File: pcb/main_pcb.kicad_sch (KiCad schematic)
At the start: 34 parts, among them J1 Conn_01x06_Socket, J2 Conn_01x10_Pin, J3 Conn_01x06_Pin, J4 USB_C_Receptacle_USB2.0, Q1 Si2323DS, SW1 SW_Push, SW2 SW_Push, SW3 SW_Push, U1 ESP32-H2-MINI-1, U2 LM5165Y

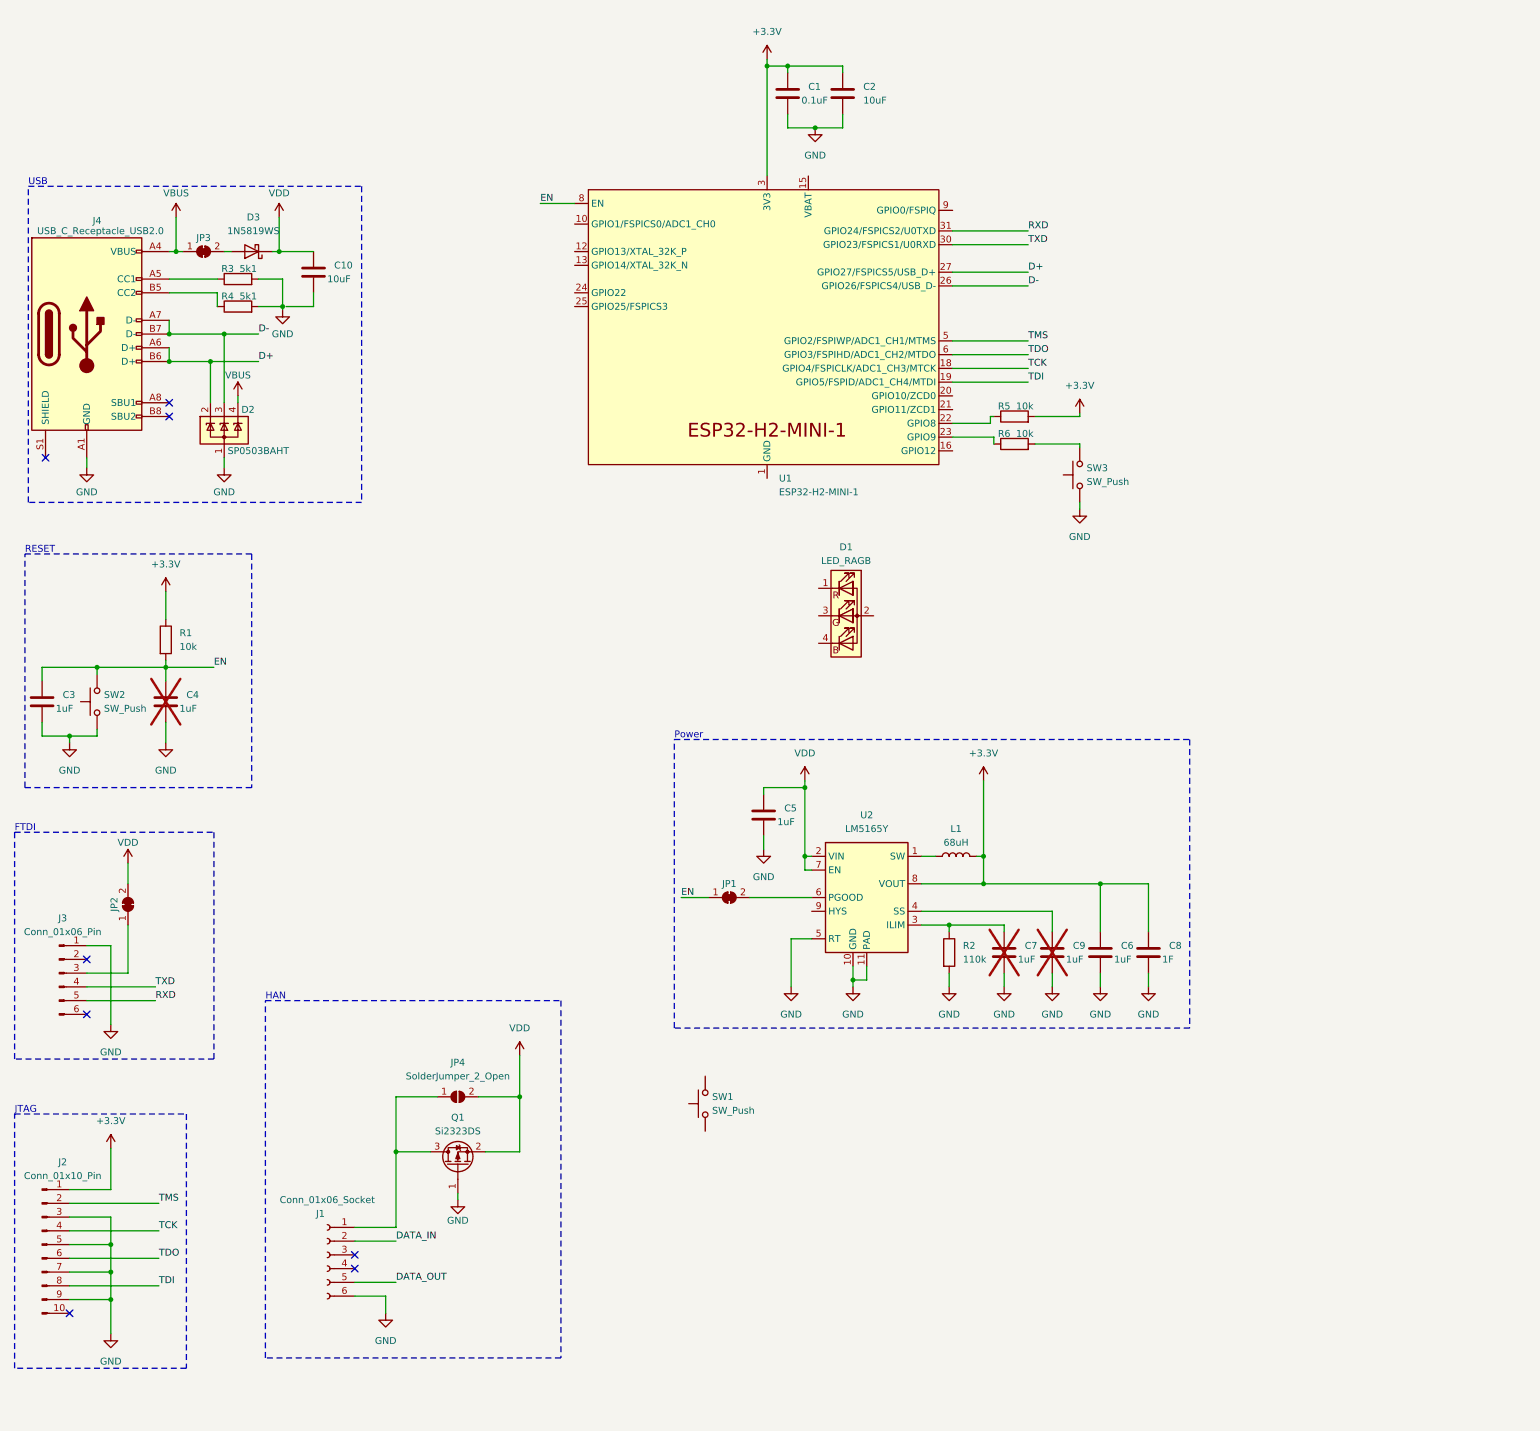
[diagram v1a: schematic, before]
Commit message: Add pair button circuit
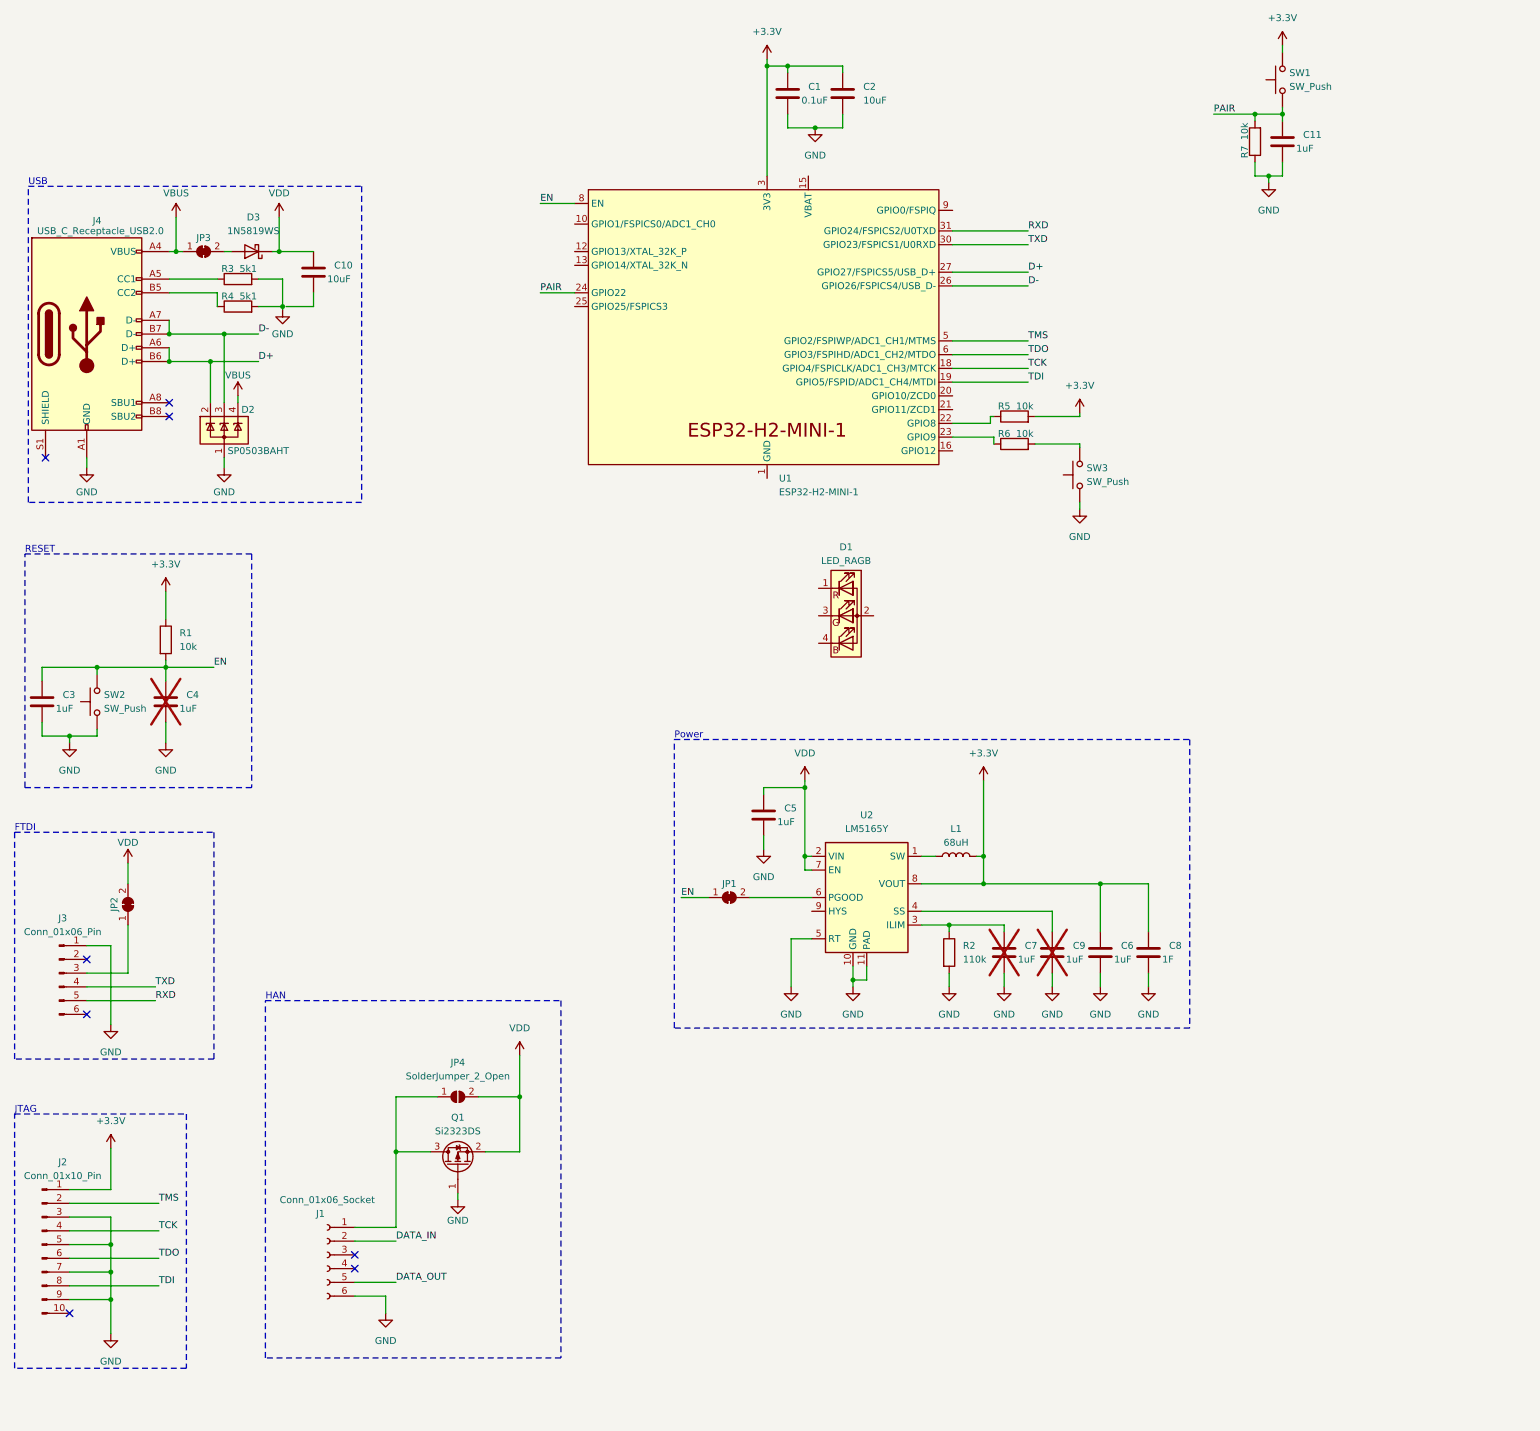
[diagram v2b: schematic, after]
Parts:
- added C11: 1uF, Capacitor_SMD:C_1206_3216Metric_Pad1.33x1.80mm_HandSolder, symbol Device:C
- added R7: 10k, Resistor_SMD:R_1206_3216Metric_Pad1.30x1.75mm_HandSolder, symbol Device:R
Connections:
- net +3.3V: now also SW1.2
- net GND: now also C11.2, R7.1
- net PAIR: now reaches U1.24 (GPIO22)
- net PAIR: now also SW1.1, C11.1, R7.2
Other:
- moved on the sheet: SW1
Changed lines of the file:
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@@
   (junction (at 34.925 140.335) (diameter 0) (color 0 0 0 0)
   )
+  (junction (at 251.46 49.53) (diameter 0) (color 0 0 0 0)
+  )
+  (junction (at 248.92 38.1) (diameter 0) (color 0 0 0 0)
+  )
   (junction (at 198.755 175.26) (diameter 0) (color 0 0 0 0)
   )
@@
   )
   (junction (at 58.42 78.74) (diameter 0) (color 0 0 0 0)
+  )
+  (junction (at 254 38.1) (diameter 0) (color 0 0 0 0)
   )
   (junction (at 198.755 180.34) (diameter 0) (color 0 0 0 0)
@@
     (stroke (width 0) (type default))
   )
+  (wire (pts (xy 254 46.99) (xy 254 49.53))
+    (stroke (width 0) (type default))
+  )
   (wire (pts (xy 58.42 78.74) (xy 58.42 91.44))
     (stroke (width 0) (type default))
@@
     (stroke (width 0) (type default))
   )
+  (wire (pts (xy 248.92 49.53) (xy 251.46 49.53))
+    (stroke (width 0) (type default))
+  )
   (wire (pts (xy 200.025 93.98) (xy 200.025 95.25))
     (stroke (width 0) (type default))
@@
     (stroke (width 0) (type default))
   )
+  (wire (pts (xy 116.84 71.12) (xy 123.19 71.12))
+    (stroke (width 0) (type default))
+  )
   (wire (pts (xy 67.31 63.5) (xy 68.58 63.5))
     (stroke (width 0) (type default))
@@
     (stroke (width 0) (type default))
   )
+  (wire (pts (xy 248.92 38.1) (xy 254 38.1))
+    (stroke (width 0) (type default))
+  )
   (wire (pts (xy 216.535 99.695) (xy 216.535 99.06))
     (stroke (width 0) (type default))
@@
     (stroke (width 0) (type default))
   )
+  (wire (pts (xy 254 25.4) (xy 254 26.67))
+    (stroke (width 0) (type default))
+  )
   (wire (pts (xy 33.02 191.77) (xy 37.465 191.77))
     (stroke (width 0) (type default))
@@
     (stroke (width 0) (type default))
   )
+  (wire (pts (xy 254 39.37) (xy 254 38.1))
+    (stroke (width 0) (type default))
+  )
   (wire (pts (xy 187.325 180.34) (xy 198.755 180.34))
     (stroke (width 0) (type default))
@@
     (stroke (width 0) (type default))
   )
+  (wire (pts (xy 248.92 39.37) (xy 248.92 38.1))
+    (stroke (width 0) (type default))
+  )
   (wire (pts (xy 48.26 63.5) (xy 49.53 63.5))
     (stroke (width 0) (type default))
@@
     (stroke (width 0) (type default))
   )
+  (wire (pts (xy 248.92 46.99) (xy 248.92 49.53))
+    (stroke (width 0) (type default))
+  )
   (wire (pts (xy 48.26 83.82) (xy 55.88 83.82))
     (stroke (width 0) (type default))
@@
     (stroke (width 0) (type default))
   )
+  (wire (pts (xy 241.3 38.1) (xy 248.92 38.1))
+    (stroke (width 0) (type default))
+  )
   (wire (pts (xy 49.53 63.5) (xy 50.8 63.5))
     (stroke (width 0) (type default))
@@
     (stroke (width 0) (type default))
   )
+  (wire (pts (xy 251.46 49.53) (xy 254 49.53))
+    (stroke (width 0) (type default))
+  )
   (wire (pts (xy 187.325 187.96) (xy 192.405 187.96))
     (stroke (width 0) (type default))
@@
     (stroke (width 0) (type default))
   )
+  (wire (pts (xy 251.46 50.8) (xy 251.46 49.53))
+    (stroke (width 0) (type default))
+  )
   (wire (pts (xy 229.235 189.23) (xy 229.235 180.34))
     (stroke (width 0) (type default))
@@
   )
   (wire (pts (xy 88.265 259.715) (xy 88.265 256.54))
+    (stroke (width 0) (type default))
+  )
+  (wire (pts (xy 254 36.83) (xy 254 38.1))
     (stroke (width 0) (type default))
   )
@@
   )
   (label "EN" (at 56.515 140.335 0) (fields_autoplaced)
+    (effects (font (size 1.27 1.27)) (justify left bottom))
+  )
+  (label "PAIR" (at 241.3 38.1 0) (fields_autoplaced)
+    (effects (font (size 1.27 1.27)) (justify left bottom))
+  )
+  (label "PAIR" (at 116.84 71.12 0) (fields_autoplaced)
     (effects (font (size 1.27 1.27)) (justify left bottom))
   )
@@
     )
   )
+  (symbol (lib_id "power:GND") (at 251.46 50.8 0) (unit 1)
+    (in_bom yes) (on_board yes) (dnp no) (fields_autoplaced)
+    (property "Reference" "#PWR032" (at 251.46 57.15 0)
+      (effects (font (size 1.27 1.27)) hide)
+    )
+    (property "Value" "GND" (at 251.46 55.88 0)
+      (effects (font (size 1.27 1.27)))
+    )
+    (property "Footprint" "" (at 251.46 50.8 0)
+      (effects (font (size 1.27 1.27)) hide)
+    )
+    (property "Datasheet" "" (at 251.46 50.8 0)
+      (effects (font (size 1.27 1.27)) hide)
+    )
+    (pin "1")
+    (instances
+      (project "main_pcb"
+        (path "/6204b7c2-8814-41ee-9243-5078f55f08d4"
+          (reference "#PWR032") (unit 1)
+        )
+      )
+    )
+  )
   (symbol (lib_id "Device:C") (at 211.455 193.04 0) (unit 1)
     (in_bom yes) (on_board yes) (dnp yes)
@@
         (path "/6204b7c2-8814-41ee-9243-5078f55f08d4"
           (reference "C9") (unit 1)
+        )
+      )
+    )
+  )
+  (symbol (lib_id "Device:R") (at 248.92 43.18 180) (unit 1)
+    (in_bom yes) (on_board yes) (dnp no)
+    (property "Reference" "R7" (at 247.015 45.085 90)
+      (effects (font (size 1.27 1.27)))
+    )
+    (property "Value" "10k" (at 247.015 41.275 90)
+      (effects (font (size 1.27 1.27)))
+    )
+    (property "Footprint" "Resistor_SMD:R_1206_3216Metric_Pad1.30x1.75mm_HandSolder" (at 250.698 43.18 90)
+      (effects (font (size 1.27 1.27)) hide)
+    )
+    (property "Datasheet" "~" (at 248.92 43.18 0)
+      (effects (font (size 1.27 1.27)) hide)
+    )
+    (pin "2")
+    (pin "1")
+    (instances
+      (project "main_pcb"
+        (path "/6204b7c2-8814-41ee-9243-5078f55f08d4"
+          (reference "R7") (unit 1)
         )
       )
@@
     )
   )
+  (symbol (lib_id "Device:C") (at 254 43.18 0) (unit 1)
+    (in_bom yes) (on_board yes) (dnp no)
+    (property "Reference" "C11" (at 257.81 41.91 0)
+      (effects (font (size 1.27 1.27)) (justify left))
+    )
+    (property "Value" "1uF" (at 256.54 44.45 0)
+      (effects (font (size 1.27 1.27)) (justify left))
+    )
+    (property "Footprint" "Capacitor_SMD:C_1206_3216Metric_Pad1.33x1.80mm_HandSolder" (at 254.9652 46.99 0)
+      (effects (font (size 1.27 1.27)) hide)
+    )
+    (property "Datasheet" "~" (at 254 43.18 0)
+      (effects (font (size 1.27 1.27)) hide)
+    )
+    (pin "2")
+    (pin "1")
+    (instances
+      (project "main_pcb"
+        (path "/6204b7c2-8814-41ee-9243-5078f55f08d4"
+          (reference "C11") (unit 1)
+        )
+      )
+    )
+  )
   (symbol (lib_id "Diode:1N5819WS") (at 63.5 63.5 180) (unit 1)
     (in_bom yes) (on_board yes) (dnp no) (fields_autoplaced)
@@
     )
   )
-  (symbol (lib_id "Switch:SW_Push") (at 147.32 220.98 90) (unit 1)
-    (in_bom yes) (on_board yes) (dnp no) (fields_autoplaced)
-    (property "Reference" "SW1" (at 148.59 219.71 90)
+  (symbol (lib_id "Switch:SW_Push") (at 254 31.75 90) (unit 1)
+    (in_bom yes) (on_board yes) (dnp no) (fields_autoplaced)
+    (property "Reference" "SW1" (at 255.27 30.48 90)
       (effects (font (size 1.27 1.27)) (justify right))
     )
-    (property "Value" "SW_Push" (at 148.59 222.25 90)
+    (property "Value" "SW_Push" (at 255.27 33.02 90)
       (effects (font (size 1.27 1.27)) (justify right))
     )
-    (property "Footprint" "Button_Switch_THT:SW_Tactile_SPST_Angled_PTS645Vx31-2LFS" (at 142.24 220.98 0)
-      (effects (font (size 1.27 1.27)) hide)
-    )
-    (property "Datasheet" "~" (at 142.24 220.98 0)
+    (property "Footprint" "Button_Switch_THT:SW_Tactile_SPST_Angled_PTS645Vx31-2LFS" (at 248.92 31.75 0)
+      (effects (font (size 1.27 1.27)) hide)
+    )
+    (property "Datasheet" "~" (at 248.92 31.75 0)
       (effects (font (size 1.27 1.27)) hide)
     )
@@
         )
       )
+    )
+  )
+  (symbol (lib_id "power:+3.3V") (at 254 25.4 0) (unit 1)
+    (in_bom yes) (on_board yes) (dnp no) (fields_autoplaced)
+    (property "Reference" "#PWR031" (at 254 29.21 0)
+      (effects (font (size 1.27 1.27)) hide)
+    )
+    (property "Value" "+3.3V" (at 254 20.32 0)
+      (effects (font (size 1.27 1.27)))
+    )
+    (property "Footprint" "" (at 254 25.4 0)
+      (effects (font (size 1.27 1.27)) hide)
+    )
+    (property "Datasheet" "" (at 254 25.4 0)
+      (effects (font (size 1.27 1.27)) hide)
+    )
+    (pin "1")
+    (instances
+      (project "main_pcb"
+        (path "/6204b7c2-8814-41ee-9243-5078f55f08d4"
+          (reference "#PWR031") (unit 1)
+        )
+      )
